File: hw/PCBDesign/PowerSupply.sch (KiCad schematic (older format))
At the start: 4 parts

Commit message: Fill out a lot of the board schematic
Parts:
- removed U? (x2): IFX27001TFV, Package_TO_SOT_SMD:TO-252-3_TabPin2, symbol Regulator_Linear:IFX27001TFV
- added C? (x7): 1uF, symbol Device:C
- added C? (x5): 100nF, symbol Device:C
- added C? (x2): 4.7uF, symbol Device:C
- added D? (x2): LED, symbol Device:LED
- added J?: USB_B_Micro, symbol Connector:USB_B_Micro
- added R? (x4): 10k, symbol Device:R_US
- added R? (x2): 1.5k, symbol Device:R_US
- added R? (x6): 100k, symbol Device:R_US
- added R?: 46.8k, symbol Device:R_US
- added R?: 1.18k, symbol Device:R_US
- added R?: 1.13k, symbol Device:R_US
- added R?: 4.12k, symbol Device:R_US
- added U? (x3): AMS1117-3.3, Package_TO_SOT_SMD:SOT-223-3_TabPin2, symbol Regulator_Linear:AMS1117-3.3
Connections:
- net labels added: CHG_CFG0, CHG_CFG1, CHG_Sense, CHG_nEN, GND, PGD_Sense, USB_+5V, USB_D+, USB_D-, V_Analog, V_Batt_Sense, V_Digital, V_Wireless
- wire segments 0 -> 152
- no-connect marks 0 -> 1
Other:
- note added: "The following resistor configuration sets the properties:\n -100mA Max Input Current DFLT (CFG0/1)\n -Input limit of 1.3A if CFG pins are overridden\n -Fast Charge Current: 0.8A\n -Termination Current Threshold: 110mA\n -Safety Timer Duration: 6.25 Hrs\n -Default to charger not enabled"
- note removed: "Change to LCSC C5446. This is a totally different package.\nThis is for the digital power supply."
- note removed: "Need to select power supply for radio"
- note removed: "Same as digital, but extra filtering for analog"
- moved on the sheet: BT?, U?

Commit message: Schematic polishing
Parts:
- added J3: ExtBatt, Connector_JST:JST_PH_B2B-PH-SM4-TB_1x02-1MP_P2.00mm_Vertical, symbol Connector_Generic:Conn_01x02
- C36, C41, C42, C43, C44, C45, C46: renamed from C?; footprint (none) -> Capacitor_SMD:C_0805_2012Metric; LCSC (none) -> C28323
- C37, C40, C47, C48, C49: renamed from C?; value 100nF -> 100n; footprint (none) -> Capacitor_SMD:C_0402_1005Metric; LCSC (none) -> C1525
- C38, C39: renamed from C?; footprint (none) -> Capacitor_SMD:C_0805_2012Metric; LCSC (none) -> C1779
- D1: renamed from D?; value LED -> LED_PGD; footprint (none) -> LED_SMD:LED_0402_1005Metric; LCSC (none) -> C72043
- D2: renamed from D?; value LED -> LED_CHG; footprint (none) -> LED_SMD:LED_0402_1005Metric; LCSC (none) -> C2286
- J2: renamed from J?; footprint (none) -> USB:Amphenol-MicroB
- R72: renamed from R?; footprint (none) -> Resistor_SMD:R_0402_1005Metric; LCSC (none) -> C25900
- R73, R74, R76, R82, R83, R84: renamed from R?; footprint (none) -> Resistor_SMD:R_0402_1005Metric; LCSC (none) -> C25741
- R75: renamed from R?; footprint (none) -> Resistor_SMD:R_0402_1005Metric; LCSC (none) -> C25792
- R77, R78: renamed from R?; footprint (none) -> Resistor_SMD:R_0402_1005Metric; LCSC (none) -> C25862
- R79, R85, R86, R87: renamed from R?; footprint (none) -> Resistor_SMD:R_0402_1005Metric; LCSC (none) -> C25744
- R80, R81: renamed from R?; footprint (none) -> Resistor_SMD:R_0402_1005Metric; LCSC (none) -> C25867
- gave numbers to parts that had none: 5
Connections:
- net GND: now also J3.2 (Pin_2)
- net vBatt: now reaches BT1.1 (+), C38.1, R84.1, U7.2 (BAT), U7.3 (BAT)
- net vBatt: now also J3.1 (Pin_1)
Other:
- moved on the sheet: BT1

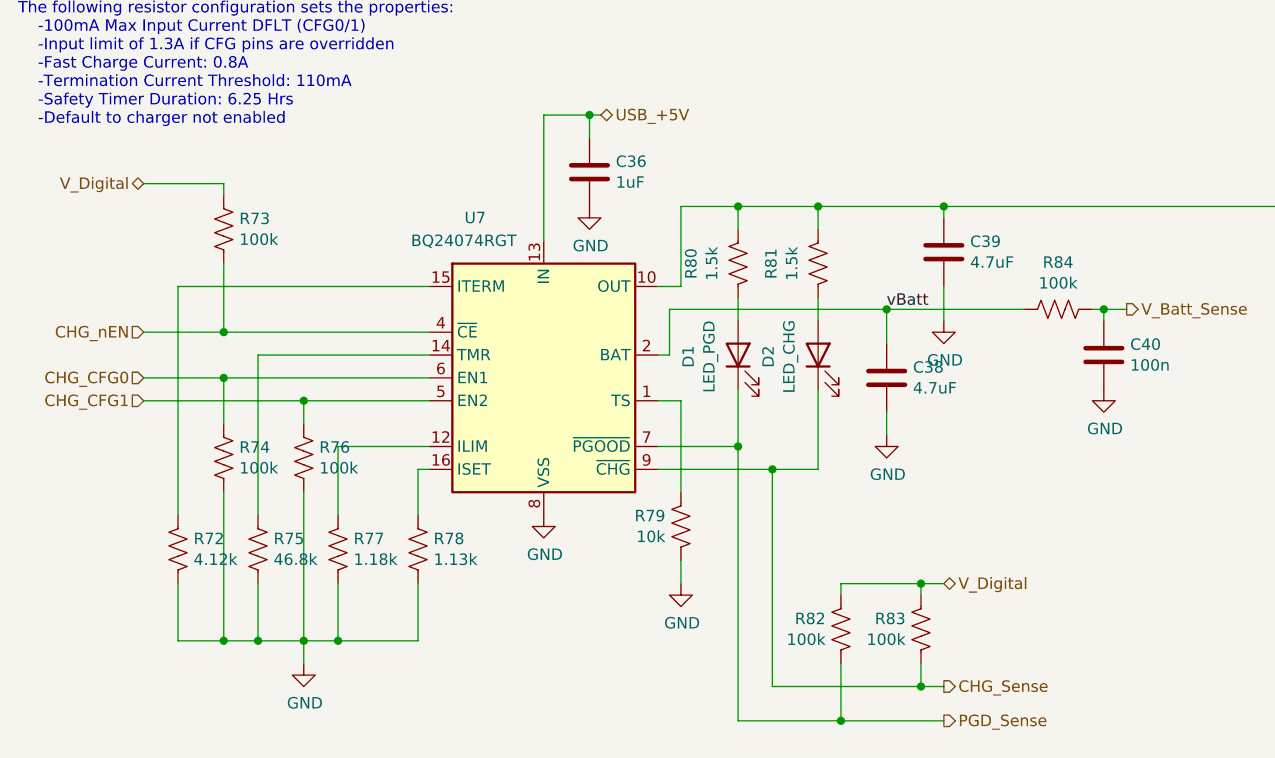
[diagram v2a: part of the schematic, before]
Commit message: Laid out power section
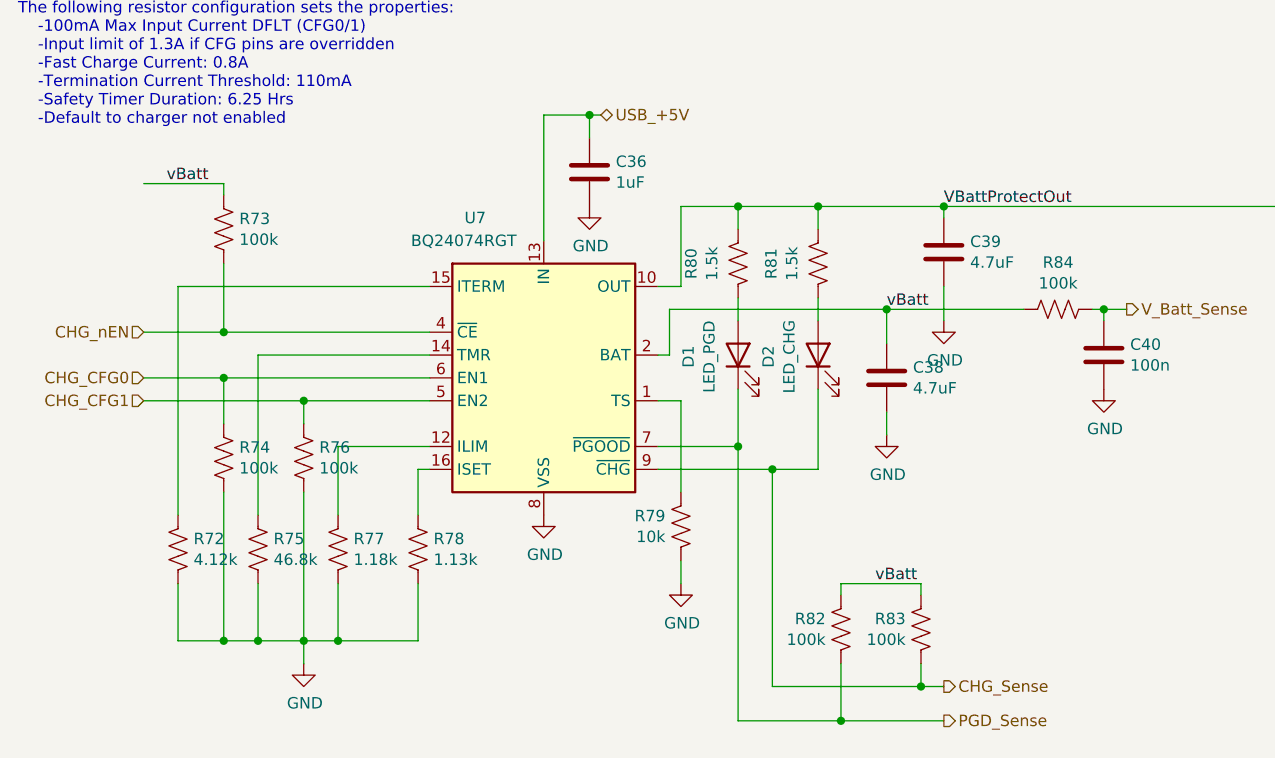
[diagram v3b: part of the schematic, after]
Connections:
- net V_Digital: no longer R73.2, R82.2, R83.2
- net vBatt: now also R73.2, R82.2, R83.2
- net VBattProtectOut: now reaches C39.1, C41.2, C42.2, C43.2, R80.2, R81.2, U10.3 (VI), U7.10 (OUT), U7.11 (OUT), U8.3 (VI), U9.3 (VI)
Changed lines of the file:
@@
 Wire Wire Line
 	5350 4450 5350 4100
-Text HLabel 5900 4950 2    50   BiDi ~ 0
-V_Digital
 $Comp
 L Device:R_US R83
@@
 	4650 4450 5150 4450
 Wire Wire Line
-	5900 4950 5800 4950
-Wire Wire Line
 	5800 4950 5800 5000
 Wire Wire Line
@@
 Wire Wire Line
 	5450 4950 5450 5000
-Connection ~ 5800 4950
 Wire Wire Line
 	5800 5300 5800 5400
@@
 Wire Wire Line
 	2750 3850 3650 3850
-Text HLabel 2400 3200 0    50   BiDi ~ 0
-V_Digital
 Wire Wire Line
 	2400 3200 2750 3200
@@
 Wire Wire Line
 	5650 3750 6250 3750
+Text Label 5900 3300 0    50   ~ 0
+VBattProtectOut
+Text Label 2500 3200 0    50   ~ 0
+vBatt
+Text Label 5600 4950 0    50   ~ 0
+vBatt
 $EndSCHEMATC

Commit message: Lay out more PCB
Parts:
- removed C42, C43, C45, C46: 1uF, Capacitor_SMD:C_0805_2012Metric, symbol Device:C
- removed C48, C49: 100n, Capacitor_SMD:C_0402_1005Metric, symbol Device:C
- removed R86, R87: 10k, Resistor_SMD:R_0402_1005Metric, symbol Device:R_US
- removed U10, U9: AMS1117-3.3, Package_TO_SOT_SMD:SOT-223-3_TabPin2, symbol Regulator_Linear:AMS1117-3.3
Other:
- moved on the sheet: C41, C44, C47, R85, U8

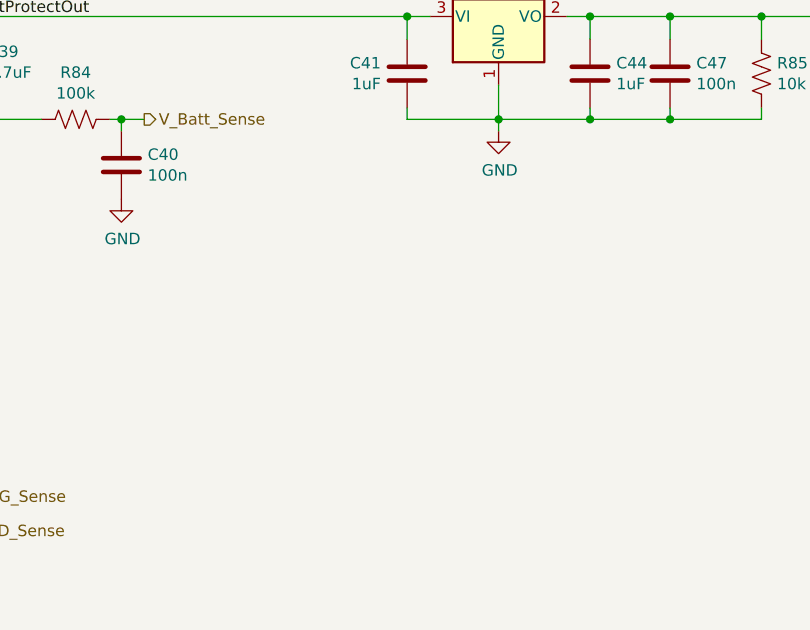
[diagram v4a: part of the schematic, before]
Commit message: Routed most of the core peripherals
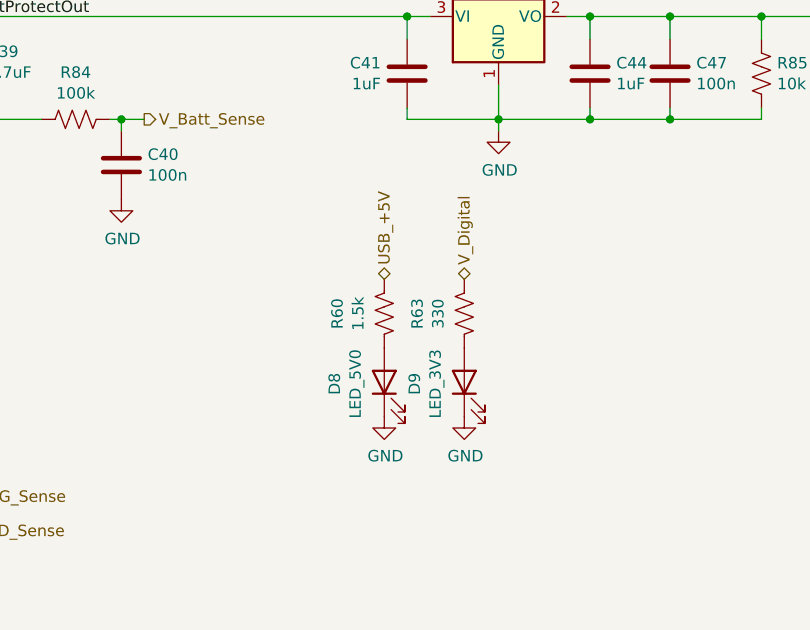
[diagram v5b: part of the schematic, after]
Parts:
- added D8: LED_5V0, LED_SMD:LED_0402_1005Metric, symbol Device:LED
- added D9: LED_3V3, LED_SMD:LED_0402_1005Metric, symbol Device:LED
- added R60: 1.5k, Resistor_SMD:R_0402_1005Metric, symbol Device:R_US
- added R63: 330, Resistor_SMD:R_0402_1005Metric, symbol Device:R_US
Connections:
- net GND: now also D8.1 (K), D9.1 (K)
- net USB_+5V: now also R60.2
- net V_Digital: now also R63.2
- new net: D9.2 (A), R63.1
- new net: D8.2 (A), R60.1
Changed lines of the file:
@@
 Wire Wire Line
 	5900 3300 7850 3300
+$Comp
+L Device:LED D9
+U 1 1 60590DC3
+P 8100 4900
+F 0 "D9" H 8093 5117 50  0000 C CNN
+F 1 "LED_3V3" H 8093 5026 50  0000 C CNN
+F 2 "LED_SMD:LED_0402_1005Metric" H 8100 4900 50  0001 C CNN
+F 3 "~" H 8100 4900 50  0001 C CNN
+F 4 "C72041" H 8100 4900 50  0001 C CNN "LCSC"
+	1    8100 4900
+	0    -1   -1   0
+$EndComp
+$Comp
+L Device:LED D8
+U 1 1 605912DA
+P 7750 4900
+F 0 "D8" H 7743 5117 50  0000 C CNN
+F 1 "LED_5V0" H 7743 5026 50  0000 C CNN
+F 2 "LED_SMD:LED_0402_1005Metric" H 7750 4900 50  0001 C CNN
+F 3 "~" H 7750 4900 50  0001 C CNN
+F 4 "C72041" H 7750 4900 50  0001 C CNN "LCSC"
+	1    7750 4900
+	0    -1   -1   0
+$EndComp
+Text HLabel 7750 4450 1    50   BiDi ~ 0
+USB_+5V
+$Comp
+L Device:R_US R60
+U 1 1 6059151B
+P 7750 4600
+F 0 "R60" V 7545 4600 50  0000 C CNN
+F 1 "1.5k" V 7636 4600 50  0000 C CNN
+F 2 "Resistor_SMD:R_0402_1005Metric" V 7790 4590 50  0001 C CNN
+F 3 "~" H 7750 4600 50  0001 C CNN
+F 4 "C25867" H 7750 4600 50  0001 C CNN "LCSC"
+	1    7750 4600
+	1    0    0    1
+$EndComp
+$Comp
+L Device:R_US R63
+U 1 1 605924E4
+P 8100 4600
+F 0 "R63" V 7895 4600 50  0000 C CNN
+F 1 "330" V 7986 4600 50  0000 C CNN
+F 2 "Resistor_SMD:R_0402_1005Metric" V 8140 4590 50  0001 C CNN
+F 3 "~" H 8100 4600 50  0001 C CNN
+F 4 "C25104" H 8100 4600 50  0001 C CNN "LCSC"
+	1    8100 4600
+	1    0    0    1
+$EndComp
+Text HLabel 8100 4450 1    50   BiDi ~ 0
+V_Digital
+$Comp
+L power:GND #PWR04
+U 1 1 60596CB2
+P 7750 5050
+F 0 "#PWR04" H 7750 4800 50  0001 C CNN
+F 1 "GND" H 7755 4877 50  0000 C CNN
+F 2 "" H 7750 5050 50  0001 C CNN
+F 3 "" H 7750 5050 50  0001 C CNN
+	1    7750 5050
+	1    0    0    -1
+$EndComp
+$Comp
+L power:GND #PWR05
+U 1 1 60596EA9
+P 8100 5050
+F 0 "#PWR05" H 8100 4800 50  0001 C CNN
+F 1 "GND" H 8105 4877 50  0000 C CNN
+F 2 "" H 8100 5050 50  0001 C CNN
+F 3 "" H 8100 5050 50  0001 C CNN
+	1    8100 5050
+	1    0    0    -1
+$EndComp
 $EndSCHEMATC

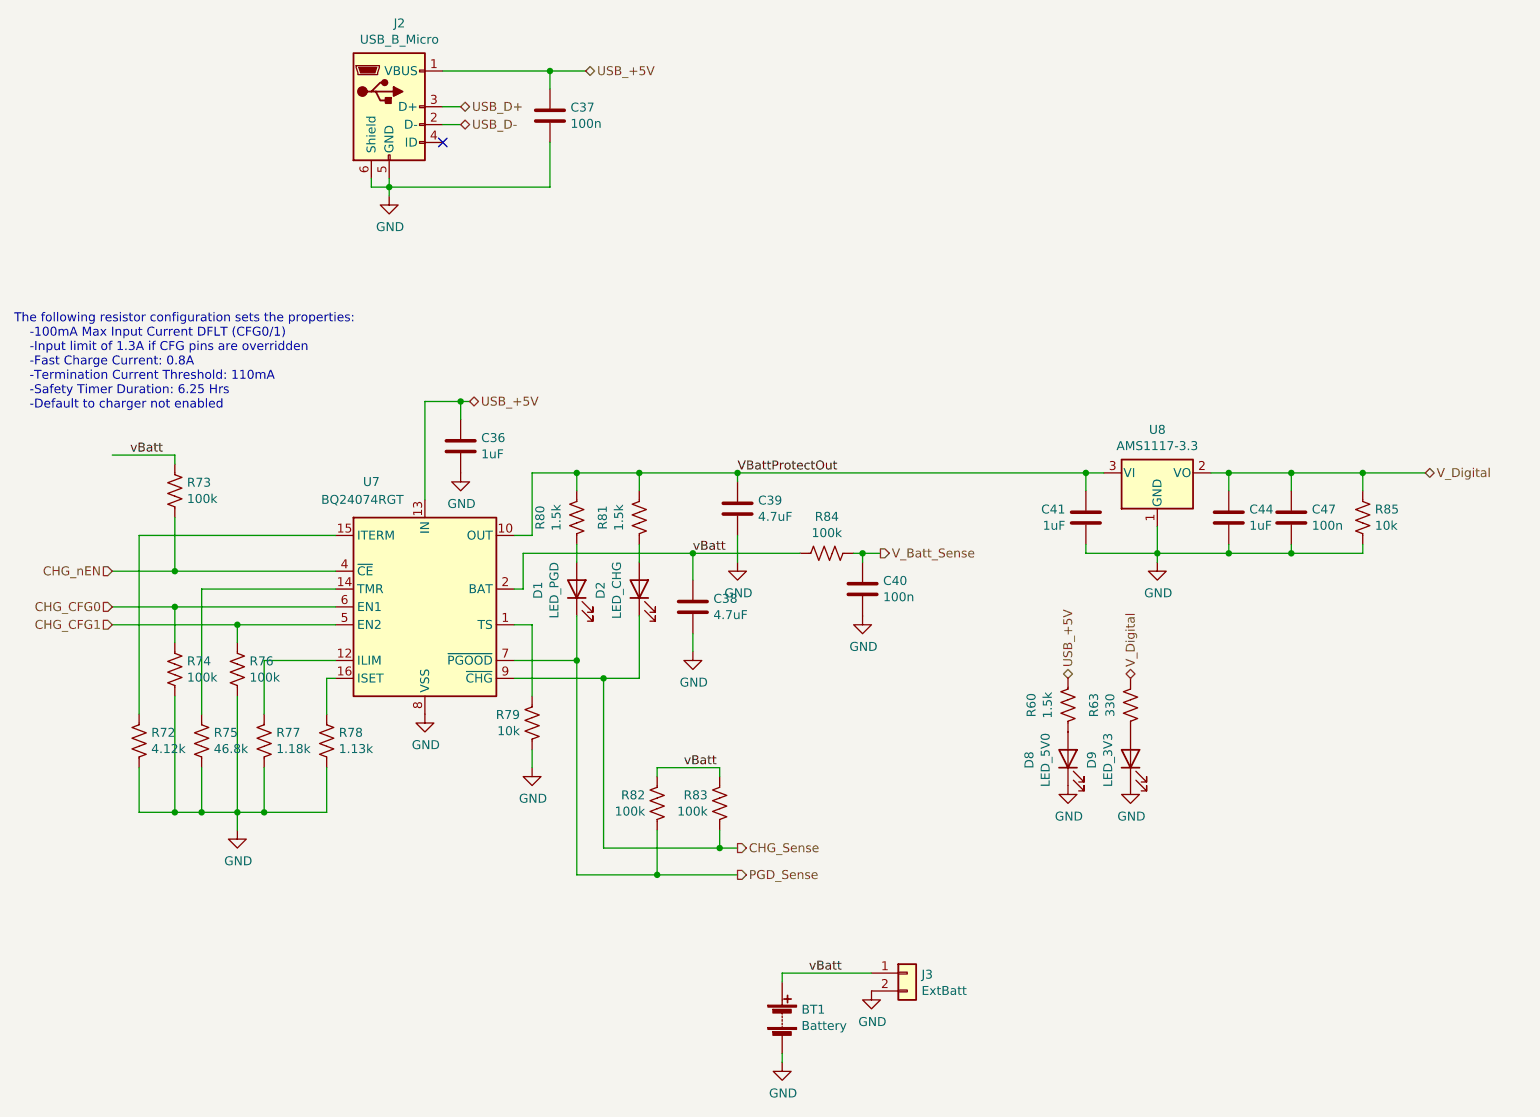
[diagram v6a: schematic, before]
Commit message: Finished preliminary route of PCB after design review checklist
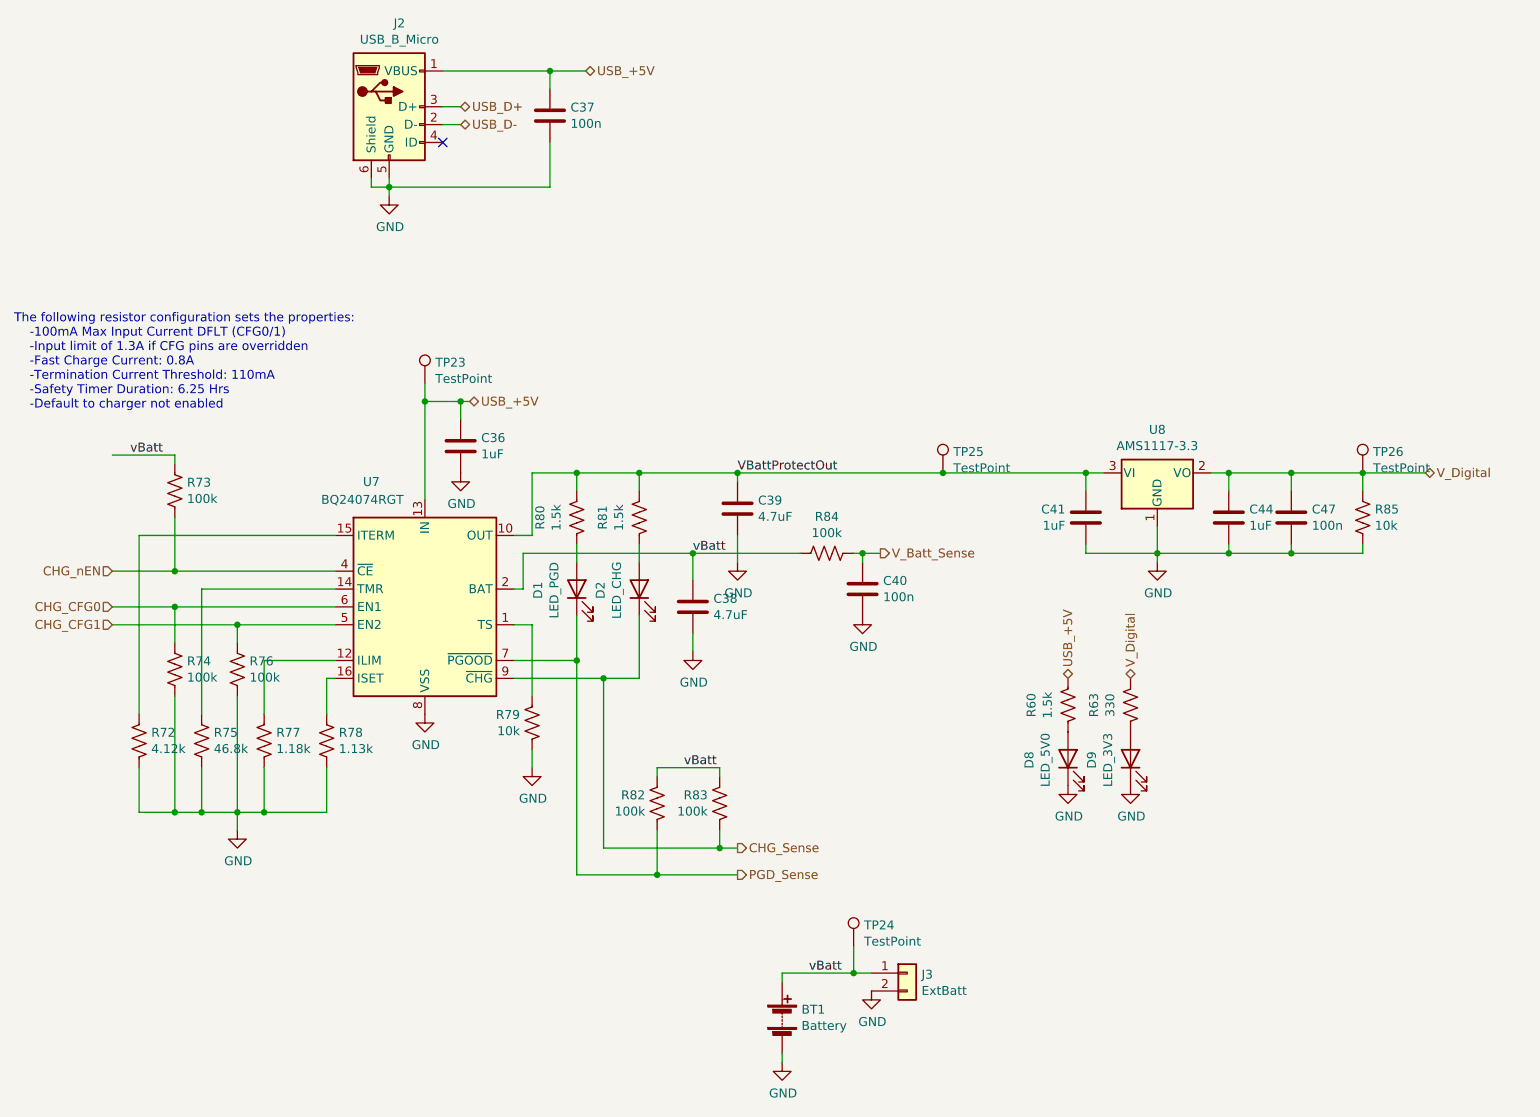
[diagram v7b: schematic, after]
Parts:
- added TP23, TP24, TP25, TP26: TestPoint, TestPoint:TestPoint_Pad_2.5x2.5mm, symbol Connector:TestPoint
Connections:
- net USB_+5V: now also TP23.1
- net VBattProtectOut: now also TP25.1
- net V_Digital: now also TP26.1
- net vBatt: now also TP24.1
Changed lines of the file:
@@
 	6150 6150 6150 6100
 Wire Wire Line
-	6150 6100 6650 6100
+	6150 6100 6550 6100
 Text Label 6300 6100 0    50   ~ 0
 vBatt
@@
 vBatt
 Wire Wire Line
-	5900 3300 7850 3300
+	5900 3300 7050 3300
 $Comp
 L Device:LED D9
@@
 Text HLabel 2400 4150 0    50   Input ~ 0
 CHG_CFG1
+$Comp
+L Connector:TestPoint TP?
+U 1 1 605E73DA
+P 6550 5950
+AR Path="/6045890B/605E73DA" Ref="TP?"  Part="1"
+AR Path="/604707FB/605E73DA" Ref="TP?"  Part="1"
+AR Path="/60472222/605E73DA" Ref="TP24"  Part="1"
+F 0 "TP24" H 6608 6068 50  0000 L CNN
+F 1 "TestPoint" H 6608 5977 50  0000 L CNN
+F 2 "TestPoint:TestPoint_Pad_2.5x2.5mm" H 6750 5950 50  0001 C CNN
+F 3 "~" H 6750 5950 50  0001 C CNN
+	1    6550 5950
+	1    0    0    -1
+$EndComp
+Wire Wire Line
+	6550 5950 6550 6100
+Connection ~ 6550 6100
+Wire Wire Line
+	6550 6100 6650 6100
+$Comp
+L Connector:TestPoint TP?
+U 1 1 605EF9F2
+P 7050 3300
+AR Path="/6045890B/605EF9F2" Ref="TP?"  Part="1"
+AR Path="/604707FB/605EF9F2" Ref="TP?"  Part="1"
+AR Path="/60472222/605EF9F2" Ref="TP25"  Part="1"
+F 0 "TP25" H 7108 3418 50  0000 L CNN
+F 1 "TestPoint" H 7108 3327 50  0000 L CNN
+F 2 "TestPoint:TestPoint_Pad_2.5x2.5mm" H 7250 3300 50  0001 C CNN
+F 3 "~" H 7250 3300 50  0001 C CNN
+	1    7050 3300
+	1    0    0    -1
+$EndComp
+Connection ~ 7050 3300
+Wire Wire Line
+	7050 3300 7850 3300
+$Comp
+L Connector:TestPoint TP?
+U 1 1 605EFDA7
+P 9400 3300
+AR Path="/6045890B/605EFDA7" Ref="TP?"  Part="1"
+AR Path="/604707FB/605EFDA7" Ref="TP?"  Part="1"
+AR Path="/60472222/605EFDA7" Ref="TP26"  Part="1"
+F 0 "TP26" H 9458 3418 50  0000 L CNN
+F 1 "TestPoint" H 9458 3327 50  0000 L CNN
+F 2 "TestPoint:TestPoint_Pad_2.5x2.5mm" H 9600 3300 50  0001 C CNN
+F 3 "~" H 9600 3300 50  0001 C CNN
+	1    9400 3300
+	1    0    0    -1
+$EndComp
+$Comp
+L Connector:TestPoint TP?
+U 1 1 605EFFE3
+P 4150 2800
+AR Path="/6045890B/605EFFE3" Ref="TP?"  Part="1"
+AR Path="/604707FB/605EFFE3" Ref="TP?"  Part="1"
+AR Path="/60472222/605EFFE3" Ref="TP23"  Part="1"
+F 0 "TP23" H 4208 2918 50  0000 L CNN
+F 1 "TestPoint" H 4208 2827 50  0000 L CNN
+F 2 "TestPoint:TestPoint_Pad_2.5x2.5mm" H 4350 2800 50  0001 C CNN
+F 3 "~" H 4350 2800 50  0001 C CNN
+	1    4150 2800
+	1    0    0    -1
+$EndComp
+Wire Wire Line
+	4150 2800 4150 2900
+Connection ~ 4150 2900
 $EndSCHEMATC
